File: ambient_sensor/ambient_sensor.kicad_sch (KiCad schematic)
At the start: 1 part

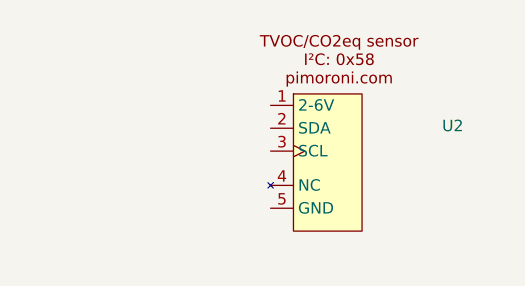
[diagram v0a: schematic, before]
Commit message: footprint and schematic for Si7021
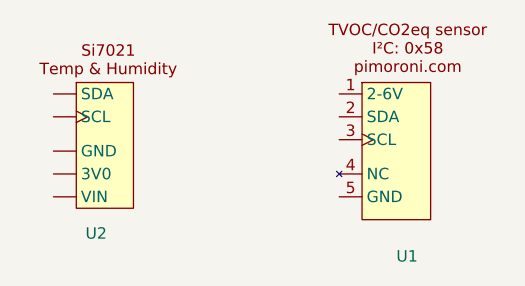
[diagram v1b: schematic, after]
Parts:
- removed U2: ~, symbol sensors:SGP30
- added U1: ~, sensors:SGP30, symbol sensors:SGP30
- added U2: ~, sensors:Si7021original, symbol sensors:Si7021Original
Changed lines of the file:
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@@
 	(paper "A4")
 	(symbol
-		(lib_id "sensors:SGP30")
-		(at 115.57 105.41 0)
+		(lib_id "sensors:Si7021Original")
+		(at 88.9 107.95 0)
 		(unit 1)
 		(exclude_from_sim no)
@@
 		(on_board yes)
 		(dnp no)
-		(fields_autoplaced yes)
 		(property "Reference" "U2"
-			(at 128.27 102.6067 0)
+			(at 88.646 114.554 0)
 			(effects
 				(font
@@
 		)
 		(property "Value" "~"
-			(at 128.27 104.5118 0)
+			(at 100.33 103.753 0)
 			(effects
 				(font
@@
 			)
 		)
-		(property "Footprint" ""
-			(at 110.49 105.41 0)
+		(property "Footprint" "sensors:Si7021original"
+			(at 90.932 113.792 0)
 			(effects
 				(font
@@
 		)
 		(property "Datasheet" ""
-			(at 110.49 105.41 0)
+			(at 88.9 107.95 0)
 			(effects
 				(font
@@
 		)
 		(property "Description" ""
-			(at 110.49 105.41 0)
+			(at 88.9 107.95 0)
 			(effects
 				(font
@@
 			)
 		)
-		(pin "3"
+		(pin ""
 		)
-		(pin "2"
+		(pin ""
 		)
-		(pin "1"
+		(pin ""
 		)
-		(pin "5"
+		(pin ""
 		)
-		(pin "4"
+		(pin ""
 		)
 		(instances
@@
 					(unit 1)
 				)
+			)
+		)
+	)
+	(symbol
+		(lib_id "sensors:SGP30")
+		(at 123.19 104.14 0)
+		(unit 1)
+		(exclude_from_sim no)
+		(in_bom yes)
+		(on_board yes)
+		(dnp no)
+		(property "Reference" "U1"
+			(at 123.19 117.094 0)
+			(effects
+				(font
+					(size 1.27 1.27)
+				)
+				(justify left)
+			)
+		)
+		(property "Value" "~"
+			(at 135.89 103.2418 0)
+			(effects
+				(font
+					(size 1.27 1.27)
+				)
+				(justify left)
+			)
+		)
+		(property "Footprint" "sensors:SGP30"
+			(at 118.11 104.14 0)
+			(effects
+				(font
+					(size 1.27 1.27)
+				)
+				(hide yes)
+			)
+		)
+		(property "Datasheet" ""
+			(at 118.11 104.14 0)
+			(effects
+				(font
+					(size 1.27 1.27)
+				)
+				(hide yes)
+			)
+		)
+		(property "Description" ""
+			(at 118.11 104.14 0)
+			(effects
+				(font
+					(size 1.27 1.27)
+				)
+				(hide yes)
+			)
+		)
+		(pin "5"
+		)
+		(pin "4"
+		)
+		(pin "3"
+		)
+		(pin "2"
+		)
+		(pin "1"
+		)
+		(instances
+			(project ""
+				(path "/9e64b25d-56eb-4d28-941d-8d1b0cd0a88c"
+					(reference "U1")
+					(unit 1)
+				)

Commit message: last modification in schema for now
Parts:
- added U3: ~, sensors:BMP280, symbol sensors:BMP280
- added U4: ATmega328-P, Package_DIP:DIP-28_W7.62mm, symbol MCU_Microchip_ATmega:ATmega328-P
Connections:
- new net: U4.22 (GND), U4.8 (GND)
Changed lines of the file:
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@@
 	(paper "A4")
+	(symbol
+		(lib_id "MCU_Microchip_ATmega:ATmega328-P")
+		(at 46.99 57.15 0)
+		(unit 1)
+		(exclude_from_sim no)
+		(in_bom yes)
+		(on_board yes)
+		(dnp no)
+		(fields_autoplaced yes)
+		(property "Reference" "U4"
+			(at 25.4 20.3514 0)
+			(effects
+				(font
+					(size 1.27 1.27)
+				)
+			)
+		)
+		(property "Value" "ATmega328-P"
+			(at 25.4 22.8914 0)
+			(effects
+				(font
+					(size 1.27 1.27)
+				)
+			)
+		)
+		(property "Footprint" "Package_DIP:DIP-28_W7.62mm"
+			(at 46.99 57.15 0)
+			(effects
+				(font
+					(size 1.27 1.27)
+					(italic yes)
+				)
+				(hide yes)
+			)
+		)
+		(property "Datasheet" "http://ww1.microchip.com/downloads/en/DeviceDoc/ATmega328_P%20AVR%20MCU%20with%20picoPower%20Technology%20Data%20Sheet%2040001984A.pdf"
+			(at 46.99 57.15 0)
+			(effects
+				(font
+					(size 1.27 1.27)
+				)
+				(hide yes)
+			)
+		)
+		(property "Description" "20MHz, 32kB Flash, 2kB SRAM, 1kB EEPROM, DIP-28"
+			(at 46.99 57.15 0)
+			(effects
+				(font
+					(size 1.27 1.27)
+				)
+				(hide yes)
+			)
+		)
+		(pin "17"
+		)
+		(pin "8"
+		)
+		(pin "16"
+		)
+		(pin "19"
+		)
+		(pin "12"
+		)
+		(pin "11"
+		)
+		(pin "13"
+		)
+		(pin "10"
+		)
+		(pin "22"
+		)
+		(pin "18"
+		)
+		(pin "1"
+		)
+		(pin "14"
+		)
+		(pin "3"
+		)
+		(pin "25"
+		)
+		(pin "9"
+		)
+		(pin "24"
+		)
+		(pin "2"
+		)
+		(pin "4"
+		)
+		(pin "21"
+		)
+		(pin "20"
+		)
+		(pin "27"
+		)
+		(pin "5"
+		)
+		(pin "23"
+		)
+		(pin "6"
+		)
+		(pin "26"
+		)
+		(pin "28"
+		)
+		(pin "7"
+		)
+		(pin "15"
+		)
+		(instances
+			(project ""
+				(path "/9e64b25d-56eb-4d28-941d-8d1b0cd0a88c"
+					(reference "U4")
+					(unit 1)
+				)
+			)
+		)
+	)
 	(symbol
 		(lib_id "sensors:Si7021Original")
@@
 					(unit 1)
 				)
+			)
+		)
+	)
+	(symbol
+		(lib_id "sensors:BMP280")
+		(at 101.6 73.66 0)
+		(unit 1)
+		(exclude_from_sim no)
+		(in_bom yes)
+		(on_board yes)
+		(dnp no)
+		(fields_autoplaced yes)
+		(property "Reference" "U3"
+			(at 102.362 49.53 0)
+			(effects
+				(font
+					(size 1.27 1.27)
+				)
+			)
+		)
+		(property "Value" "~"
+			(at 102.362 52.07 0)
+			(effects
+				(font
+					(size 1.27 1.27)
+				)
+			)
+		)
+		(property "Footprint" "sensors:BMP280"
+			(at 102.616 51.308 0)
+			(effects
+				(font
+					(size 1.27 1.27)
+				)
+				(hide yes)
+			)
+		)
+		(property "Datasheet" ""
+			(at 101.6 73.66 0)
+			(effects
+				(font
+					(size 1.27 1.27)
+				)
+				(hide yes)
+			)
+		)
+		(property "Description" ""
+			(at 101.6 73.66 0)
+			(effects
+				(font
+					(size 1.27 1.27)
+				)
+				(hide yes)
+			)
+		)
+		(pin "3"
+		)
+		(pin "6"
+		)
+		(pin "5"
+		)
+		(pin "4"
+		)
+		(pin "2"
+		)
+		(pin "1"
+		)
+		(pin "7"
+		)
+		(instances
+			(project ""
+				(path "/9e64b25d-56eb-4d28-941d-8d1b0cd0a88c"
+					(reference "U3")
+					(unit 1)
+				)

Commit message: clock
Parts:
- added Y1: Crystal, Crystal:Resonator-2Pin_W10.0mm_H5.0mm, symbol Device:Crystal
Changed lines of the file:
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@@
+	)
+	(symbol
+		(lib_id "Device:Crystal")
+		(at 134.62 52.07 0)
+		(unit 1)
+		(exclude_from_sim no)
+		(in_bom yes)
+		(on_board yes)
+		(dnp no)
+		(fields_autoplaced yes)
+		(property "Reference" "Y1"
+			(at 134.62 44.45 0)
+			(effects
+				(font
+					(size 1.27 1.27)
+				)
+			)
+		)
+		(property "Value" "Crystal"
+			(at 134.62 46.99 0)
+			(effects
+				(font
+					(size 1.27 1.27)
+				)
+			)
+		)
+		(property "Footprint" "Crystal:Resonator-2Pin_W10.0mm_H5.0mm"
+			(at 134.62 52.07 0)
+			(effects
+				(font
+					(size 1.27 1.27)
+				)
+				(hide yes)
+			)
+		)
+		(property "Datasheet" "~"
+			(at 134.62 52.07 0)
+			(effects
+				(font
+					(size 1.27 1.27)
+				)
+				(hide yes)
+			)
+		)
+		(property "Description" "Two pin crystal"
+			(at 134.62 52.07 0)
+			(effects
+				(font
+					(size 1.27 1.27)
+				)
+				(hide yes)
+			)
+		)
+		(pin "2"
+		)
+		(pin "1"
+		)
+		(instances
+			(project ""
+				(path "/9e64b25d-56eb-4d28-941d-8d1b0cd0a88c"
+					(reference "Y1")
+					(unit 1)
+				)
+			)
+		)
 	)
 	(symbol

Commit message: schema
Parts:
- removed Y1: Crystal, Crystal:Resonator-2Pin_W10.0mm_H5.0mm, symbol Device:Crystal
- added R1, R2: 4.7k, symbol Device:R
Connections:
- net 5v: now reaches U4.20 (AVCC)
- net 5v: now also U1.1 (2-6V), U2. (VIN), U3.1 (VIN), U3.2 (3Vo), U4.7 (VCC)
- net GND: now reaches U4.22 (GND), U4.8 (GND)
- net GND: now also U1.5 (GND), U2. (VIN), U3.3 (GND)
- net at U4.27 (PC4): now also U2. (VIN), R1.2
- net at U4.28 (PC5): now also U1.3 (SCL), U2. (VIN), U3.5 (SDO), R2.2
- net at U1.2 (SDA): now also U3.6 (SDI)
- new net input: R1.1, R2.1
- no-connect marks 0 -> 25
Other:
- moved on the sheet: U1, U2, U3, U4

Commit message: C and R
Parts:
- added C1: C, Capacitor_SMD:C_1206_3216Metric, symbol Device:C
- added Y1: Crystal, Crystal:Resonator-2Pin_W10.0mm_H5.0mm, symbol Device:Crystal
- R2: footprint (none) -> Resistor_SMD:R_1206_3216Metric
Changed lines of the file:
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@@
+	)
+	(symbol
+		(lib_id "Device:C")
+		(at 210.82 90.17 0)
+		(unit 1)
+		(exclude_from_sim no)
+		(in_bom yes)
+		(on_board yes)
+		(dnp no)
+		(fields_autoplaced yes)
+		(property "Reference" "C1"
+			(at 214.63 88.8999 0)
+			(effects
+				(font
+					(size 1.27 1.27)
+				)
+				(justify left)
+			)
+		)
+		(property "Value" "C"
+			(at 214.63 91.4399 0)
+			(effects
+				(font
+					(size 1.27 1.27)
+				)
+				(justify left)
+			)
+		)
+		(property "Footprint" "Capacitor_SMD:C_1206_3216Metric"
+			(at 211.7852 93.98 0)
+			(effects
+				(font
+					(size 1.27 1.27)
+				)
+				(hide yes)
+			)
+		)
+		(property "Datasheet" "~"
+			(at 210.82 90.17 0)
+			(effects
+				(font
+					(size 1.27 1.27)
+				)
+				(hide yes)
+			)
+		)
+		(property "Description" "Unpolarized capacitor"
+			(at 210.82 90.17 0)
+			(effects
+				(font
+					(size 1.27 1.27)
+				)
+				(hide yes)
+			)
+		)
+		(pin "2"
+		)
+		(pin "1"
+		)
+		(instances
+			(project ""
+				(path "/9e64b25d-56eb-4d28-941d-8d1b0cd0a88c"
+					(reference "C1")
+					(unit 1)
+				)
+			)
+		)
 	)
 	(symbol
@@
 	)
 	(symbol
+		(lib_id "Device:Crystal")
+		(at 69.85 95.25 0)
+		(unit 1)
+		(exclude_from_sim no)
+		(in_bom yes)
+		(on_board yes)
+		(dnp no)
+		(fields_autoplaced yes)
+		(property "Reference" "Y1"
+			(at 69.85 87.63 0)
+			(effects
+				(font
+					(size 1.27 1.27)
+				)
+			)
+		)
+		(property "Value" "Crystal"
+			(at 69.85 90.17 0)
+			(effects
+				(font
+					(size 1.27 1.27)
+				)
+			)
+		)
+		(property "Footprint" "Crystal:Resonator-2Pin_W10.0mm_H5.0mm"
+			(at 69.85 95.25 0)
+			(effects
+				(font
+					(size 1.27 1.27)
+				)
+				(hide yes)
+			)
+		)
+		(property "Datasheet" "~"
+			(at 69.85 95.25 0)
+			(effects
+				(font
+					(size 1.27 1.27)
+				)
+				(hide yes)
+			)
+		)
+		(property "Description" "Two pin crystal"
+			(at 69.85 95.25 0)
+			(effects
+				(font
+					(size 1.27 1.27)
+				)
+				(hide yes)
+			)
+		)
+		(pin "2"
+		)
+		(pin "1"
+		)
+		(instances
+			(project "ambient_sensor"
+				(path "/9e64b25d-56eb-4d28-941d-8d1b0cd0a88c"
+					(reference "Y1")
+					(unit 1)
+				)
+			)
+		)
+	)
+	(symbol
 		(lib_id "Device:R")
 		(at 88.9 45.72 0)
@@
 			)
 		)
-		(property "Footprint" ""
+		(property "Footprint" "Resistor_SMD:R_1206_3216Metric"
 			(at 87.122 45.72 90)
 			(effects

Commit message: clock
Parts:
- added C2: 22p, Capacitor_SMD:C_1206_3216Metric, symbol Device:C
- C1: value C -> 22p
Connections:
- net GND: now also C1.2, C2.2
- net at U4.10 (XTAL2/PB7): now also Y1.1, C2.1
- net at U4.9 (XTAL1/PB6): now also C1.1, Y1.2
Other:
- moved on the sheet: C1, R1, R2, Y1

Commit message: addittional components
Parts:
- added U6: LD1117S33TR_SOT223, Package_TO_SOT_SMD:SOT-223-3_TabPin2, symbol Regulator_Linear:LD1117S33TR_SOT223
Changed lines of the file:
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@@
+	)
+	(symbol
+		(lib_id "Regulator_Linear:LD1117S33TR_SOT223")
+		(at 181.61 97.79 0)
+		(unit 1)
+		(exclude_from_sim no)
+		(in_bom yes)
+		(on_board yes)
+		(dnp no)
+		(fields_autoplaced yes)
+		(property "Reference" "U6"
+			(at 181.61 91.44 0)
+			(effects
+				(font
+					(size 1.27 1.27)
+				)
+			)
+		)
+		(property "Value" "LD1117S33TR_SOT223"
+			(at 181.61 93.98 0)
+			(effects
+				(font
+					(size 1.27 1.27)
+				)
+			)
+		)
+		(property "Footprint" "Package_TO_SOT_SMD:SOT-223-3_TabPin2"
+			(at 181.61 92.71 0)
+			(effects
+				(font
+					(size 1.27 1.27)
+				)
+				(hide yes)
+			)
+		)
+		(property "Datasheet" "http://www.st.com/st-web-ui/static/active/en/resource/technical/document/datasheet/CD00000544.pdf"
+			(at 184.15 104.14 0)
+			(effects
+				(font
+					(size 1.27 1.27)
+				)
+				(hide yes)
+			)
+		)
+		(property "Description" "800mA Fixed Low Drop Positive Voltage Regulator, Fixed Output 3.3V, SOT-223"
+			(at 181.61 97.79 0)
+			(effects
+				(font
+					(size 1.27 1.27)
+				)
+				(hide yes)
+			)
+		)
+		(pin "2"
+		)
+		(pin "1"
+		)
+		(pin "3"
+		)
+		(instances
+			(project ""
+				(path "/9e64b25d-56eb-4d28-941d-8d1b0cd0a88c"
+					(reference "U6")
+					(unit 1)
+				)
+			)
+		)
 	)
 	(symbol

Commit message: clock and reset
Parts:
- added C3: 10u, Capacitor_SMD:C_1206_3216Metric, symbol Device:C
- added J1: Conn_01x02_Pin, Connector_PinHeader_2.54mm:PinHeader_1x02_P2.54mm_Vertical, symbol Connector:Conn_01x02_Pin
- added R3: 10k, Resistor_SMD:R_1206_3216Metric, symbol Device:R
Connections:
- net GND: now also U6.1 (GND), C3.1, J1.1 (Pin_1)
- net at U4.1 (~{RESET}/PC6): now also J1.2 (Pin_2), R3.1
- net +4V: now reaches U4.21 (AREF)
- net +4V: now also U1.1 (2-6V), U2. (VIN), U3.1 (VIN), U3.2 (3Vo), U4.20 (AVCC), U4.7 (VCC), U6.2 (VO), C3.2, R3.2
- removed net 5v: U1.1 (2-6V), U2. (VIN), U3.1 (VIN), U3.2 (3Vo), U4.20 (AVCC), U4.7 (VCC)
